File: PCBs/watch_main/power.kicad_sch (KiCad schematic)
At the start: 12 parts, among them IC201 ADP5360ACBZ-2-R7, IC202 ADP5301ACBZ-2-R7

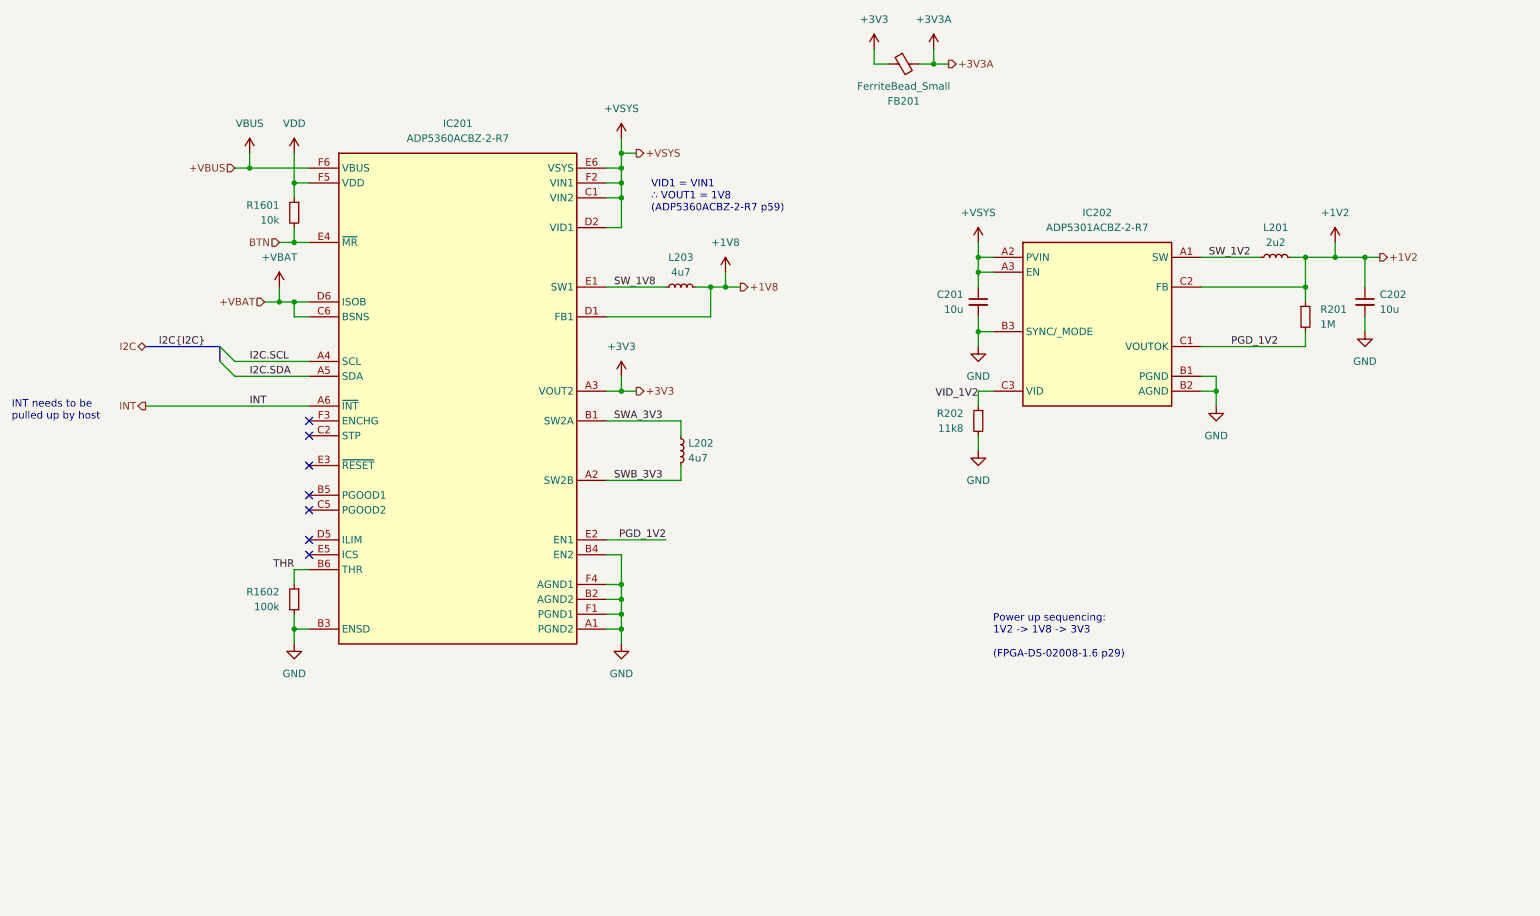
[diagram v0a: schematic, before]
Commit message: Created firmware project
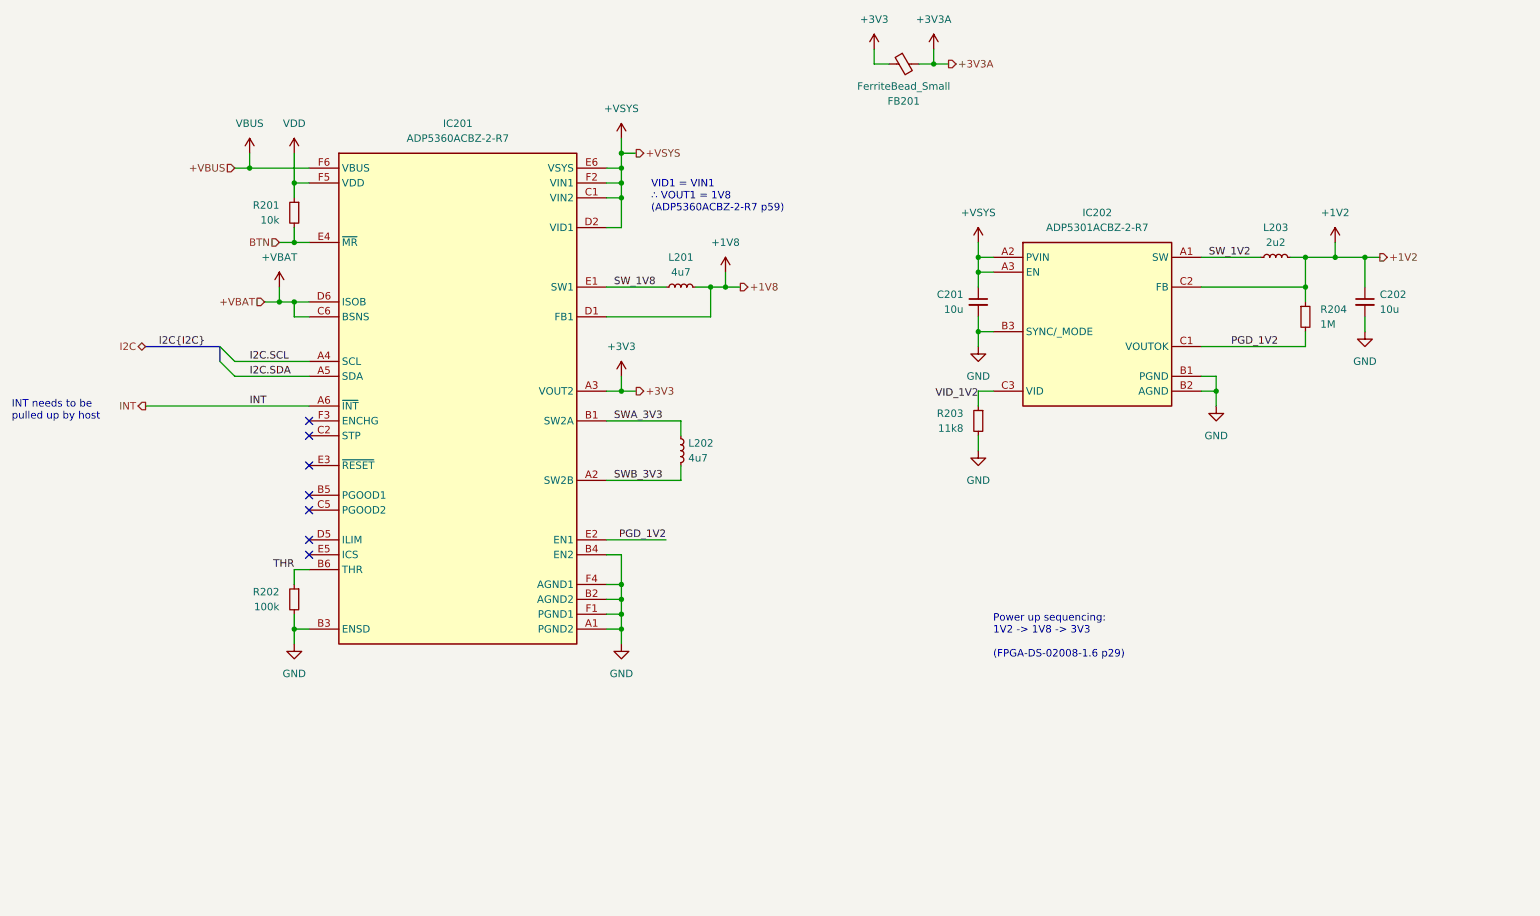
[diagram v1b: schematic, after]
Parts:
- renumbered L203 to L201, L201 to L203, R1601 to R201, R1602 to R202, R202 to R203, R201 to R204

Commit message: Progress with schematic and RFID simulations
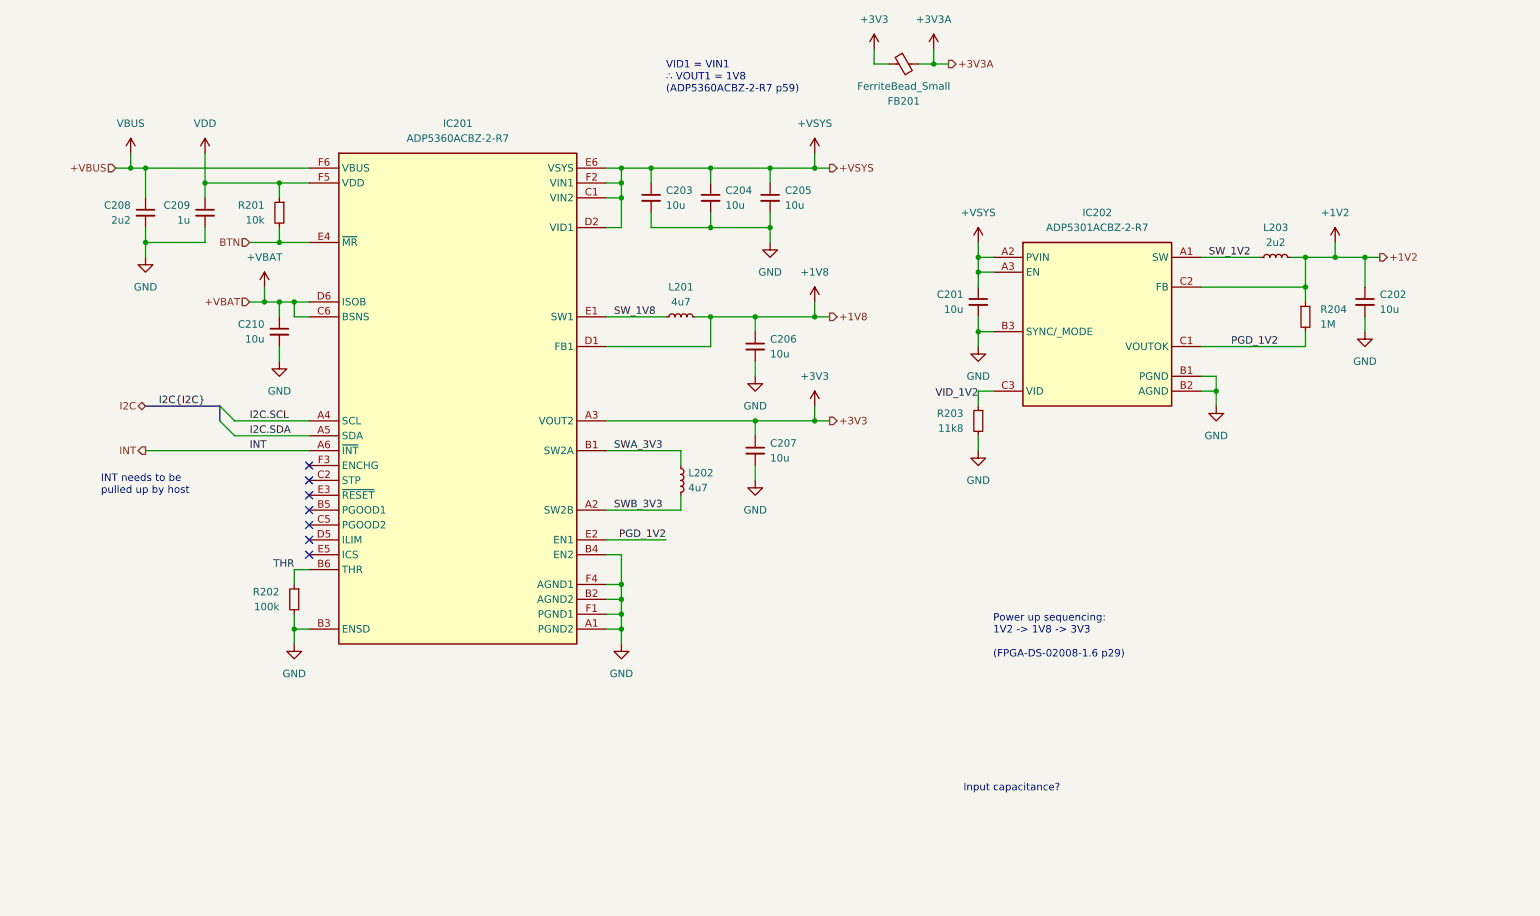
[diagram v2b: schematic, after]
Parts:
- added C203, C204, C205, C206, C207, C210: 10u, Capacitor_SMD:C_0402_1005Metric, symbol Device:C_Small
- added C208: 2u2, Capacitor_SMD:C_0402_1005Metric, symbol Device:C_Small
- added C209: 1u, Capacitor_SMD:C_0402_1005Metric, symbol Device:C_Small
- C201, C202: footprint Capacitor_SMD:C_0603_1608Metric -> Capacitor_SMD:C_0402_1005Metric
- IC202: Manufacturer_Part_Number ADP5301ACBZ-3-R7 -> ADP5301ACBZ-2-R7
- L201, L202, L203: footprint (none) -> Inductor_SMD:L_0805_2012Metric
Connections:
- net +1V8: now also C206.1
- net +3V3: now also C207.1
- net +VBAT: now also C210.1
- net +VSYS: now also C203.1, C204.1, C205.1
- net GND: now also C203.2, C204.2, C205.2, C206.2, C207.2, C208.2, C209.2, C210.2
- net VBUS: now also C208.1
- net VDD: now also C209.1
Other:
- note added: "Input capacitance?"
- moved on the sheet: R201

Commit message: Schematic finished and BOM started
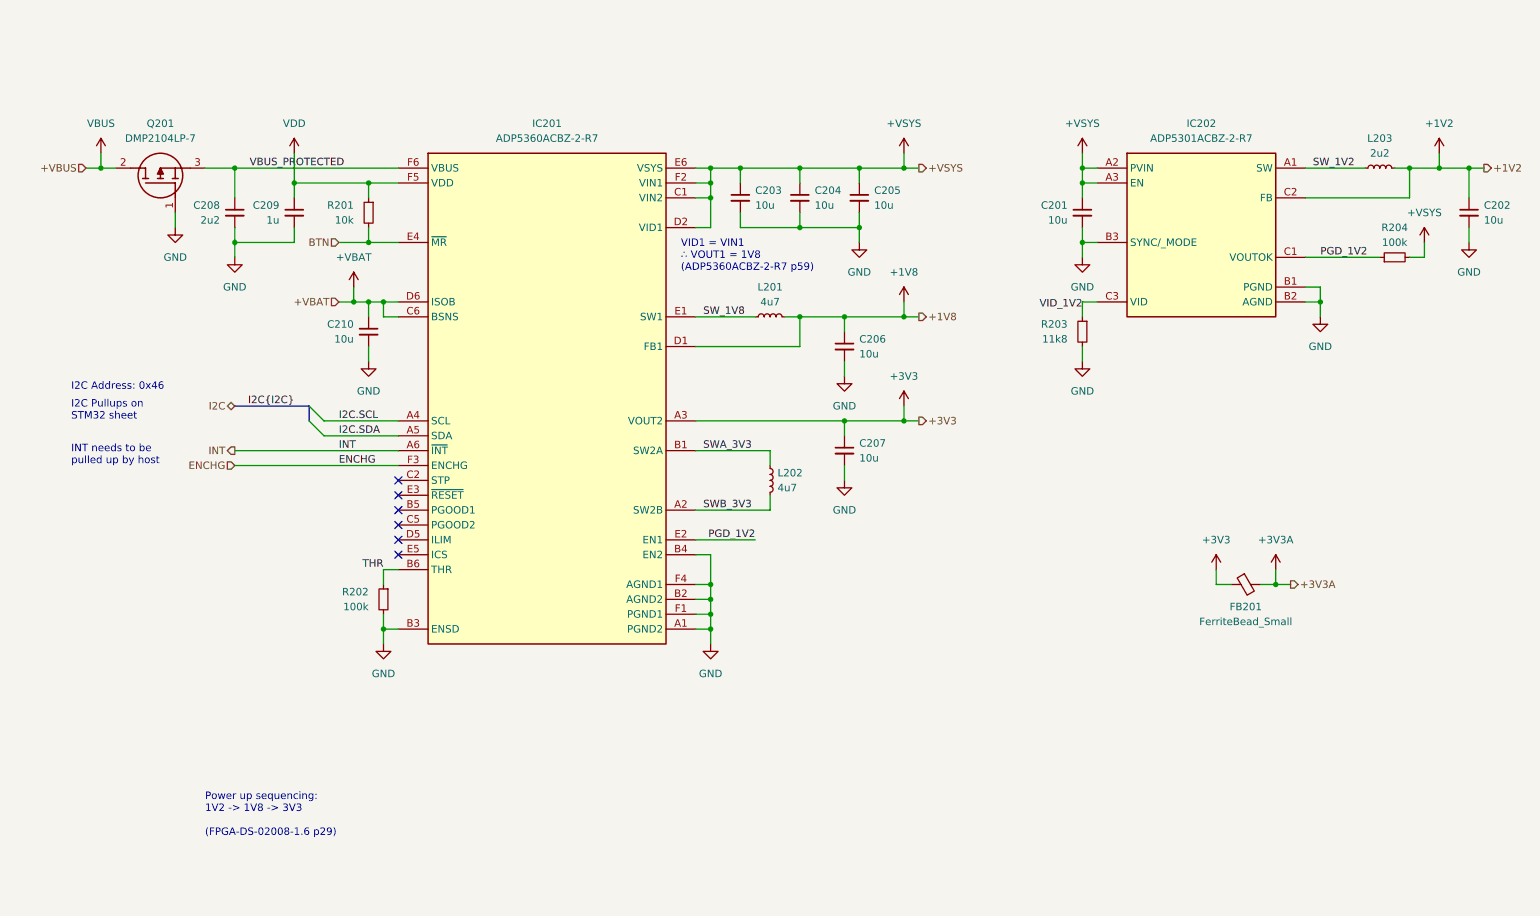
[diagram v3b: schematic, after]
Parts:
- added Q201: DMP2104LP-7, watch_footprints:DMP2104LP7, symbol DMP2104LP-7:DMP2104LP-7
- L201, L202: footprint Inductor_SMD:L_0805_2012Metric -> Inductor_SMD:L_Murata_DFE201610P
- L203: footprint Inductor_SMD:L_0805_2012Metric -> Inductor_SMD:L_TDK_MLZ1608
- R204: value 1M -> 100k
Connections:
- net +1V2: no longer R204.1
- net +VSYS: now also R204.2
- net GND: now also Q201.1 (G)
- net PGD_1V2: now also R204.1; no longer R204.2
- net VBUS: now also Q201.2 (D); no longer C208.1, IC201.F6 (VBUS)
- net ENCHG: now reaches IC201.F3 (ENCHG)
- new net VBUS_PROTECTED: C208.1, IC201.F6 (VBUS), Q201.3 (S)
- no-connect marks 7 -> 6
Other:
- note added: "I2C Address: 0x46"
- note added: "I2C Pullups on STM32 sheet"
- note removed: "Input capacitance?"
- title: (none) -> Watch Power
- moved on the sheet: C201, C202, C203, C204, C205, C206, C207, C208, C209, C210, FB201, IC201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

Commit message: Created test rig schematic
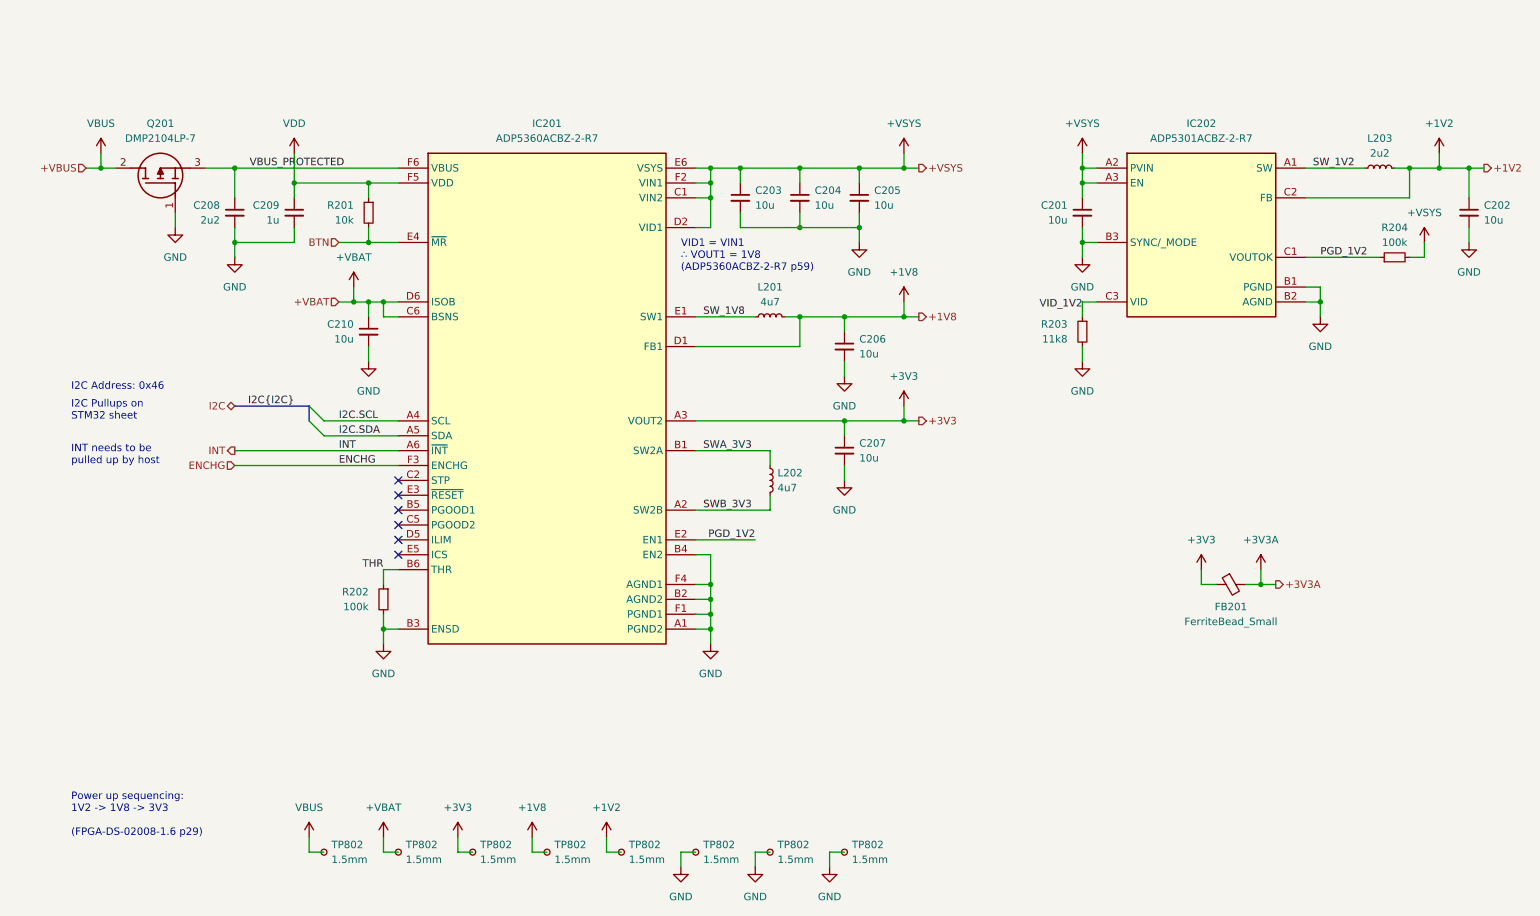
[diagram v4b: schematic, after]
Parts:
- added TP802 (x8): 1.5mm, TestPoint:TestPoint_Pad_D1.5mm, symbol Connector:TestPoint_Small
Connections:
- net +1V2: now also TP802.1
- net +1V8: now also TP802.1
- net +3V3: now also TP802.1
- net +VBAT: now also TP802.1
- net GND: now also TP802.1, TP802.1, TP802.1
- net VBUS: now also TP802.1
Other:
- moved on the sheet: FB201

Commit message: Started routing main PCB
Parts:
- renumbered C208 to C201, C209 to C202, C210 to C203, C203 to C204, C204 to C205, C205 to C208, C201 to C209, C202 to C210

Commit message: 224 Unrouted traces
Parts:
- added TP802: 1.5mm, TestPoint:TestPoint_Pad_D1.5mm, symbol Connector:TestPoint_Small
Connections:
- net GND: now also TP802.1
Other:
- moved on the sheet: TP802

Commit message: 69 Unrouted traces
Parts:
- removed FB201: FerriteBead_Small, Resistor_SMD:R_0402_1005Metric, symbol Device:FerriteBead_Small
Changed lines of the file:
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@@
   (junction (at 160.02 88.9) (diameter 0) (color 0 0 0 0)
-  )
-  (junction (at 231.14 134.62) (diameter 0) (color 0 0 0 0)
   )
   (junction (at 137.16 137.16) (diameter 0) (color 0 0 0 0)
@@
     (stroke (width 0) (type default))
   )
-  (wire (pts (xy 228.6 134.62) (xy 231.14 134.62))
-    (stroke (width 0) (type default))
-  )
-  (wire (pts (xy 231.14 132.08) (xy 231.14 134.62))
-    (stroke (width 0) (type default))
-  )
   (wire (pts (xy 30.48 63.5) (xy 33.02 63.5))
     (stroke (width 0) (type default))
@@
     (stroke (width 0) (type default))
   )
-  (wire (pts (xy 231.14 134.62) (xy 233.68 134.62))
-    (stroke (width 0) (type default))
-  )
   (wire (pts (xy 200.66 76.2) (xy 203.2 76.2))
     (stroke (width 0) (type default))
@@
     (stroke (width 0) (type default))
   )
-  (wire (pts (xy 220.98 132.08) (xy 220.98 134.62))
-    (stroke (width 0) (type default))
-  )
   (wire (pts (xy 152.4 93.98) (xy 152.4 88.9))
     (stroke (width 0) (type default))
@@
   )
   (wire (pts (xy 78.74 66.04) (xy 78.74 68.58))
-    (stroke (width 0) (type default))
-  )
-  (wire (pts (xy 220.98 134.62) (xy 223.52 134.62))
     (stroke (width 0) (type default))
   )
@@
   )
   (hierarchical_label "+1V8" (shape output) (at 172.72 88.9 0) (fields_autoplaced)
-    (effects (font (size 1.27 1.27)) (justify left))
-  )
-  (hierarchical_label "+3V3A" (shape output) (at 233.68 134.62 0) (fields_autoplaced)
     (effects (font (size 1.27 1.27)) (justify left))
   )
@@
     )
   )
-  (symbol (lib_id "Device:FerriteBead_Small") (at 226.06 134.62 90) (mirror x) (unit 1)
-    (in_bom yes) (on_board yes) (dnp no)
-    (property "Reference" "FB201" (at 226.0219 138.43 90)
-      (effects (font (size 1.27 1.27)))
-    )
-    (property "Value" "FerriteBead_Small" (at 226.0219 140.97 90)
-      (effects (font (size 1.27 1.27)))
-    )
-    (property "Footprint" "Resistor_SMD:R_0402_1005Metric" (at 226.06 132.842 90)
-      (effects (font (size 1.27 1.27)) hide)
-    )
-    (property "Datasheet" "~" (at 226.06 134.62 0)
-      (effects (font (size 1.27 1.27)) hide)
-    )
-    (pin "1")
-    (pin "2")
-    (instances
-      (project "watch_main"
-        (path "/b008648a-c7cf-4e14-8a0a-b9314d757b4a/8f996a8c-7777-4a55-b361-37cede76953f"
-          (reference "FB201") (unit 1)
-        )
-      )
-    )
-  )
   (symbol (lib_id "power:VBUS") (at 33.02 60.96 0) (unit 1)
     (in_bom yes) (on_board yes) (dnp no) (fields_autoplaced)
@@
     )
   )
-  (symbol (lib_id "watch_symbols_lib:+3V3A") (at 231.14 132.08 0) (unit 1)
-    (in_bom yes) (on_board yes) (dnp no) (fields_autoplaced)
-    (property "Reference" "#PWR0227" (at 231.14 135.89 0)
-      (effects (font (size 1.27 1.27)) hide)
-    )
-    (property "Value" "+3V3A" (at 231.14 127 0)
-      (effects (font (size 1.27 1.27)))
-    )
-    (property "Footprint" "" (at 231.14 132.08 0)
-      (effects (font (size 1.27 1.27)) hide)
-    )
-    (property "Datasheet" "" (at 231.14 132.08 0)
-      (effects (font (size 1.27 1.27)) hide)
-    )
-    (pin "1")
-    (instances
-      (project "watch_main"
-        (path "/b008648a-c7cf-4e14-8a0a-b9314d757b4a/8f996a8c-7777-4a55-b361-37cede76953f"
-          (reference "#PWR0227") (unit 1)
-        )
-      )
-    )
-  )
   (symbol (lib_id "power:GND") (at 200.66 78.74 0) (unit 1)
     (in_bom yes) (on_board yes) (dnp no)
@@
         )
       )
-    )
-  )
-  (symbol (lib_id "power:+3V3") (at 220.98 132.08 0) (unit 1)
-    (in_bom yes) (on_board yes) (dnp no) (fields_autoplaced)
-    (property "Reference" "#PWR0226" (at 220.98 135.89 0)
-      (effects (font (size 1.27 1.27)) hide)
-    )
-    (property "Value" "+3V3" (at 220.98 127 0)
-      (effects (font (size 1.27 1.27)))
-    )
-    (property "Footprint" "" (at 220.98 132.08 0)
-      (effects (font (size 1.27 1.27)) hide)
-    )
-    (property "Datasheet" "" (at 220.98 132.08 0)
-      (effects (font (size 1.27 1.27)) hide)
-    )
-    (pin "1")
-    (instances
-      (project "watch_main"
-        (path "/b008648a-c7cf-4e14-8a0a-b9314d757b4a/8f996a8c-7777-4a55-b361-37cede76953f"
-          (reference "#PWR0226") (unit 1)
-        )
-      )

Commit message: Test rig board finished
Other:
- moved on the sheet: C201, C202, C203, C204, C205, C206, C207, C208, C209, C210, IC201, IC202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
